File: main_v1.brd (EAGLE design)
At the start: 79.4 x 80.6 mm, 44 parts, among them IC1 MEGA8-P, IC2 7805TV, IC4 MC33063/MC34063P, IC5 MAX6921, IC6 MAX6921

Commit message: Fix some trace widths
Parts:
- R13: device resistor:0204V -> resistor:0207/10
- moved R13 23.5 mm to (29.5, 58.4), turned to 270 degrees
- moved R15 0.32 mm to (31.4, 70.5)
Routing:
- net ESP_RST: track 38.2 -> 33.7 mm
- net VCC: track 194.7 -> 191.3 mm
- net GND: track 312.2 -> 311.6 mm
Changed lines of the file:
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@@
 <setting verticaltext="up"/>
 </settings>
-<grid distance="0.025" unitdist="inch" unit="inch" style="dots" multiple="1" display="yes" altdistance="0.0125" altunitdist="inch" altunit="inch"/>
+<grid distance="0.025" unitdist="inch" unit="inch" style="dots" multiple="1" display="no" altdistance="0.0125" altunitdist="inch" altunit="inch"/>
 <layers>
 <layer number="1" name="Top" color="4" fill="1" visible="no" active="yes"/>
@@
 <attribute name="VALUE" x="72.6694" y="63.6524" size="0.9906" layer="27" ratio="10"/>
 </element>
-<element name="R13" library="resistor" package="0204V" value="" x="34.925" y="35.56" rot="R180"/>
+<element name="R13" library="resistor" package="0207/10" value="" x="29.5275" y="58.42" smashed="yes" rot="R270">
+<attribute name="NAME" x="29.1465" y="60.198" size="1.27" layer="25" ratio="10" rot="R270"/>
+<attribute name="VALUE" x="28.8925" y="60.6806" size="1.27" layer="27" ratio="10" rot="R270"/>
+</element>
 <element name="R14" library="resistor" package="0204/7" value="" x="29.845" y="48.26" smashed="yes">
 <attribute name="NAME" x="28.575" y="47.6504" size="0.9906" layer="25" ratio="10"/>
 <attribute name="VALUE" x="28.2194" y="47.7774" size="0.9906" layer="27" ratio="10"/>
 </element>
-<element name="R15" library="resistor" package="0204/7" value="4k7" x="31.115" y="70.485" smashed="yes" rot="R270">
-<attribute name="NAME" x="30.3784" y="71.9836" size="1.27" layer="25" ratio="10" rot="R270"/>
-<attribute name="VALUE" x="28.8036" y="72.6186" size="1.27" layer="27" ratio="10" rot="R270"/>
+<element name="R15" library="resistor" package="0204/7" value="4k7" x="31.4325" y="70.485" smashed="yes" rot="R270">
+<attribute name="NAME" x="30.6959" y="71.9836" size="1.27" layer="25" ratio="10" rot="R270"/>
+<attribute name="VALUE" x="29.1211" y="72.6186" size="1.27" layer="27" ratio="10" rot="R270"/>
 </element>
 <element name="R16" library="resistor" package="0204/7" value="4k7" x="26.3525" y="46.355" smashed="yes">
@@
 <attribute name="VALUE" x="24.7269" y="45.8724" size="0.9906" layer="27" ratio="10"/>
 </element>
-<element name="ICSP_ESP" library="con-lstb" package="MA05-1" value="" x="33.02" y="58.42" rot="R90">
+<element name="ICSP_ESP" library="con-lstb" package="MA05-1" value="" x="33.02" y="58.42" smashed="yes" rot="R90">
 <attribute name="OC_NEWARK" value="unknown" x="33.02" y="58.42" size="1.778" layer="27" rot="R90" display="off"/>
 <attribute name="MPN" value="" x="33.02" y="58.42" size="1.778" layer="27" rot="R90" display="off"/>
 <attribute name="MF" value="" x="33.02" y="58.42" size="1.778" layer="27" rot="R90" display="off"/>
 <attribute name="OC_FARNELL" value="unknown" x="33.02" y="58.42" size="1.778" layer="27" rot="R90" display="off"/>
+<attribute name="NAME" x="35.814" y="59.055" size="1.27" layer="25" ratio="10" rot="R90"/>
+<attribute name="VALUE" x="35.941" y="55.88" size="1.27" layer="27" ratio="10" rot="R90"/>
 </element>
 <element name="ESP8266" library="adafruit" package="2X04" value="" x="33.655" y="41.91" smashed="yes" rot="R270">
@@
 <via x="26.67" y="21.59" extent="1-16" drill="0.8128" diameter="1.27" shape="octagon"/>
 <wire x1="26.67" y1="33.655" x2="26.67" y2="21.59" width="0.4064" layer="1"/>
-<wire x1="29.845" y1="72.39" x2="29.845" y2="68.58" width="0.4064" layer="16"/>
+<wire x1="29.845" y1="71.755" x2="29.845" y2="68.58" width="0.4064" layer="16"/>
 <contactref element="IC3" pad="6"/>
 <via x="24.13" y="6.35" extent="1-16" drill="0.8128" diameter="1.27" shape="octagon"/>
 <wire x1="29.845" y1="68.58" x2="29.21" y2="67.945" width="0.4064" layer="16"/>
-<wire x1="29.21" y1="67.945" x2="29.21" y2="53.0225" width="0.4064" layer="16"/>
+<wire x1="29.21" y1="67.945" x2="29.21" y2="63.5" width="0.4064" layer="16"/>
+<wire x1="29.21" y1="63.5" x2="29.21" y2="54.9275" width="0.4064" layer="16"/>
+<wire x1="29.21" y1="54.9275" x2="27.94" y2="53.6575" width="0.4064" layer="16"/>
+<wire x1="27.94" y1="53.6575" x2="27.94" y2="51.7525" width="0.4064" layer="16"/>
 <wire x1="24.13" y1="6.35" x2="24.13" y2="27.94" width="0.4064" layer="1"/>
 <via x="24.13" y="27.94" extent="1-16" drill="0.8128" diameter="1.27" shape="octagon"/>
@@
 <wire x1="35.56" y1="31.75" x2="37.1475" y2="31.75" width="0.4064" layer="16"/>
 <wire x1="37.1475" y1="31.75" x2="38.4175" y2="33.02" width="0.4064" layer="16"/>
-<wire x1="35.56" y1="31.75" x2="34.6075" y2="32.7025" width="0.4064" layer="16"/>
-<wire x1="34.6075" y1="32.7025" x2="31.4325" y2="35.8775" width="0.4064" layer="16"/>
+<wire x1="35.56" y1="31.75" x2="31.4325" y2="35.8775" width="0.4064" layer="16"/>
 <wire x1="31.4325" y1="35.8775" x2="30.48" y2="36.83" width="0.4064" layer="16"/>
 <wire x1="30.48" y1="36.83" x2="25.4" y2="36.83" width="0.4064" layer="16"/>
@@
 <wire x1="38.735" y1="74.295" x2="37.465" y2="75.565" width="0.4064" layer="16"/>
 <wire x1="37.465" y1="75.565" x2="34.29" y2="75.565" width="0.4064" layer="16"/>
-<wire x1="34.29" y1="75.565" x2="31.75" y2="75.565" width="0.4064" layer="16"/>
+<wire x1="34.29" y1="75.565" x2="32.0675" y2="75.565" width="0.4064" layer="16"/>
 <wire x1="22.5425" y1="46.355" x2="25.24125" y2="49.05375" width="0.4064" layer="16"/>
-<wire x1="25.24125" y1="49.05375" x2="29.21" y2="53.0225" width="0.4064" layer="16"/>
-<wire x1="36.195" y1="35.56" x2="36.195" y2="34.29" width="0.4064" layer="16"/>
-<wire x1="36.195" y1="34.29" x2="34.6075" y2="32.7025" width="0.4064" layer="16"/>
+<wire x1="25.24125" y1="49.05375" x2="27.94" y2="51.7525" width="0.4064" layer="16"/>
 <wire x1="22.5425" y1="46.355" x2="22.5425" y2="45.72" width="0.4064" layer="16"/>
 <wire x1="26.035" y1="48.26" x2="25.24125" y2="49.05375" width="0.4064" layer="16"/>
@@
 <wire x1="32.385" y1="38.1" x2="32.385" y2="36.83" width="0.4064" layer="16"/>
 <wire x1="32.385" y1="36.83" x2="31.4325" y2="35.8775" width="0.4064" layer="16"/>
-<wire x1="29.845" y1="72.39" x2="31.115" y2="73.66" width="0.4064" layer="16"/>
-<wire x1="31.115" y1="73.66" x2="31.115" y2="74.295" width="0.4064" layer="16"/>
-<wire x1="31.115" y1="74.93" x2="31.75" y2="75.565" width="0.4064" layer="16"/>
-<wire x1="31.115" y1="74.93" x2="31.115" y2="74.295" width="0.4064" layer="16"/>
+<wire x1="29.845" y1="71.755" x2="31.4325" y2="73.3425" width="0.4064" layer="16"/>
+<wire x1="31.4325" y1="73.3425" x2="31.4325" y2="74.295" width="0.4064" layer="16"/>
+<wire x1="31.4325" y1="74.93" x2="32.0675" y2="75.565" width="0.4064" layer="16"/>
+<wire x1="31.4325" y1="74.93" x2="31.4325" y2="74.295" width="0.4064" layer="16"/>
+<wire x1="29.5275" y1="63.5" x2="29.21" y2="63.5" width="0.4064" layer="16"/>
 </signal>
 <signal name="GND">
@@
 <wire x1="34.29" y1="73.025" x2="36.83" y2="73.025" width="0.4064" layer="16"/>
 <wire x1="34.29" y1="64.77" x2="33.655" y2="65.405" width="0.4064" layer="16"/>
-<wire x1="33.655" y1="65.405" x2="30.48" y2="65.405" width="0.4064" layer="16"/>
-<wire x1="30.48" y1="65.405" x2="29.845" y2="66.04" width="0.4064" layer="16"/>
-<wire x1="29.845" y1="66.04" x2="29.845" y2="67.31" width="0.4064" layer="16"/>
-<wire x1="29.845" y1="67.31" x2="30.48" y2="67.945" width="0.4064" layer="16"/>
-<wire x1="30.48" y1="67.945" x2="33.02" y2="67.945" width="0.4064" layer="16"/>
+<wire x1="33.655" y1="65.405" x2="30.7975" y2="65.405" width="0.4064" layer="16"/>
+<wire x1="30.7975" y1="65.405" x2="30.1625" y2="66.04" width="0.4064" layer="16"/>
+<wire x1="30.1625" y1="66.04" x2="30.1625" y2="67.31" width="0.4064" layer="16"/>
+<wire x1="30.1625" y1="67.31" x2="30.7975" y2="67.945" width="0.4064" layer="16"/>
+<wire x1="30.7975" y1="67.945" x2="33.02" y2="67.945" width="0.4064" layer="16"/>
 <wire x1="33.02" y1="67.945" x2="34.29" y2="69.215" width="0.4064" layer="16"/>
 <wire x1="34.29" y1="69.215" x2="34.29" y2="73.025" width="0.4064" layer="16"/>
@@
 <wire x1="36.83" y1="44.1325" x2="36.83" y2="41.275" width="0.4064" layer="16"/>
 <wire x1="36.83" y1="41.275" x2="36.195" y2="40.64" width="0.4064" layer="16"/>
-<wire x1="31.115" y1="66.675" x2="33.655" y2="66.675" width="0.4064" layer="16"/>
+<wire x1="31.4325" y1="66.675" x2="33.655" y2="66.675" width="0.4064" layer="16"/>
 </signal>
 <signal name="ESP_RST">
 <contactref element="ICSP_ESP" pad="5"/>
-<wire x1="33.02" y1="39.37" x2="32.385" y2="39.37" width="0.4064" layer="16"/>
-<wire x1="32.385" y1="39.37" x2="27.94" y2="39.37" width="0.4064" layer="16"/>
+<wire x1="31.115" y1="39.37" x2="27.94" y2="39.37" width="0.4064" layer="16"/>
 <wire x1="27.94" y1="39.37" x2="26.9875" y2="40.3225" width="0.4064" layer="16"/>
 <wire x1="26.9875" y1="40.3225" x2="26.9875" y2="46.0375" width="0.4064" layer="16"/>
@@
 <contactref element="R13" pad="2"/>
 <contactref element="ESP8266" pad="5"/>
-<wire x1="33.655" y1="35.56" x2="33.655" y2="38.735" width="0.4064" layer="16"/>
-<wire x1="33.02" y1="39.37" x2="33.655" y2="38.735" width="0.4064" layer="16"/>
-<wire x1="32.385" y1="40.64" x2="32.385" y2="39.37" width="0.4064" layer="16"/>
+<wire x1="32.385" y1="40.64" x2="31.115" y2="39.37" width="0.4064" layer="16"/>
 <wire x1="33.02" y1="63.5" x2="31.75" y2="63.5" width="0.4064" layer="16"/>
 <wire x1="31.75" y1="63.5" x2="30.48" y2="62.23" width="0.4064" layer="16"/>
-<wire x1="30.48" y1="62.23" x2="30.48" y2="49.53" width="0.4064" layer="16"/>
+<wire x1="30.48" y1="62.23" x2="30.48" y2="53.34" width="0.4064" layer="16"/>
+<wire x1="30.48" y1="53.34" x2="30.48" y2="49.53" width="0.4064" layer="16"/>
+<wire x1="29.5275" y1="53.34" x2="30.48" y2="53.34" width="0.4064" layer="16"/>
 </signal>
 </signals>

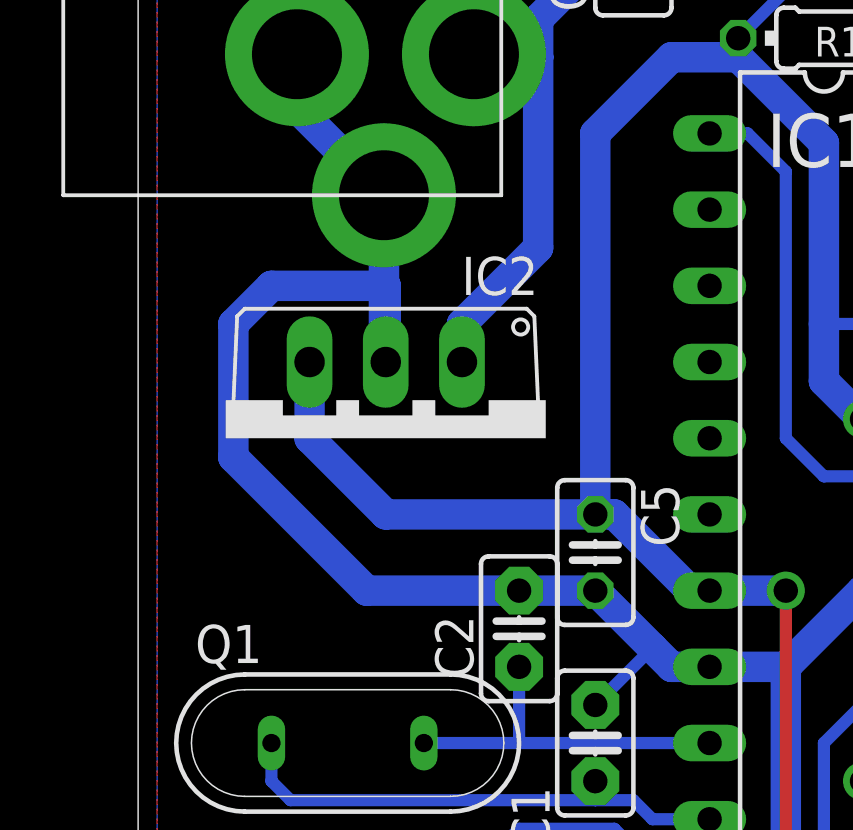
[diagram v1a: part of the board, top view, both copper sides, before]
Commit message: Replace LM7805 with LD33v
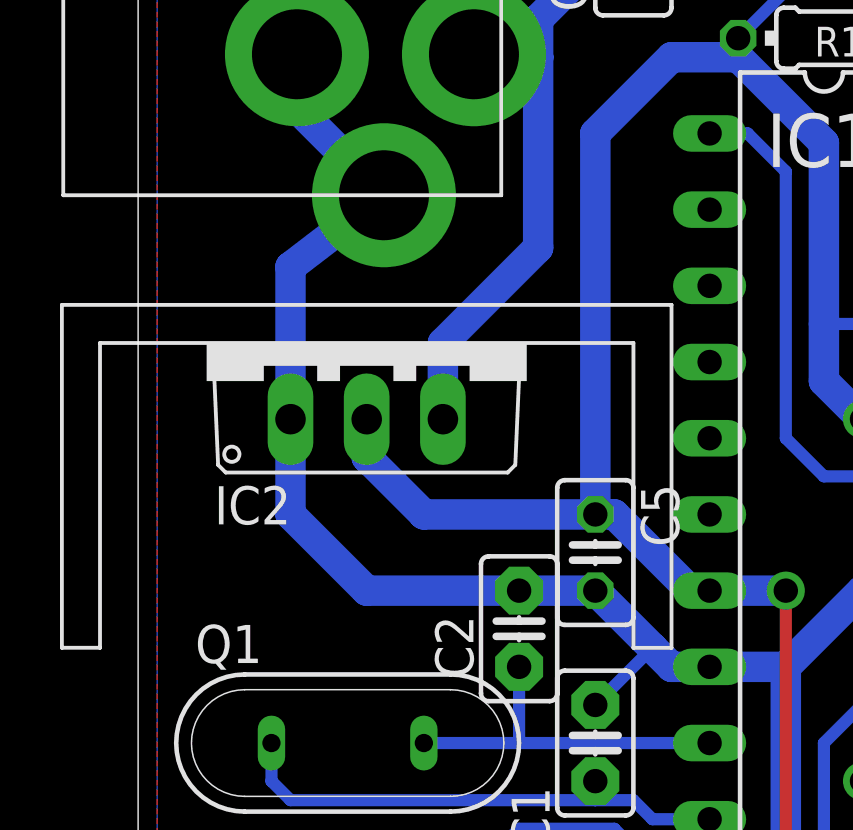
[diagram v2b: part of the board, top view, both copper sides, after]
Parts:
- IC2: value 7805TV -> LD33V05TV; device linear:TO220V -> ld33v:TO220V
- moved IC2 3.24 mm to (10.2, 36.2), turned to 0 degrees
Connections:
- net +5V: now also IC2.3; no longer IC2.1
- net GND: now also IC2.1; no longer IC2.2
- net VCC: now also IC2.2; no longer IC2.3
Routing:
- net GND: track 311.6 -> 302.9 mm
- net VCC: track 191.3 -> 187.9 mm
- net +5V: track 53.3 -> 55.4 mm
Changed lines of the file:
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@@
 <grid distance="0.025" unitdist="inch" unit="inch" style="dots" multiple="1" display="no" altdistance="0.0125" altunitdist="inch" altunit="inch"/>
 <layers>
-<layer number="1" name="Top" color="4" fill="1" visible="no" active="yes"/>
+<layer number="1" name="Top" color="4" fill="1" visible="yes" active="yes"/>
 <layer number="2" name="Route2" color="1" fill="3" visible="no" active="no"/>
 <layer number="3" name="Route3" color="4" fill="3" visible="no" active="no"/>
@@
 <attribute name="VALUE" x="22.987" y="57.023" size="1.27" layer="27" ratio="10" rot="R180"/>
 </element>
-<element name="IC2" library="linear" package="TO220V" value="7805TV" x="10.795" y="33.02" rot="R180"/>
 <element name="DCIN" library="adafruit" package="PJ-102A" value="2.1MMJACKTHM" x="4.445" y="45.72" rot="R90"/>
 <element name="C15" library="resistor" package="C025-025X050" value="" x="19.05" y="49.53" rot="R90"/>
@@
 <attribute name="VALUE" x="29.21" y="46.99" size="1.27" layer="27" rot="R270"/>
 </element>
+<element name="IC2" library="ld33v" package="TO220V" value="LD33V05TV" x="10.16" y="36.195"/>
 </elements>
 <signals>
@@
 <contactref element="C4" pad="1"/>
 <contactref element="C3" pad="1"/>
-<contactref element="IC2" pad="3"/>
-<wire x1="8.255" y1="35.56" x2="8.255" y2="33.02" width="1.016" layer="16"/>
-<wire x1="8.255" y1="33.02" x2="10.795" y2="30.48" width="1.016" layer="16"/>
-<wire x1="10.795" y1="30.48" x2="17.78" y2="30.48" width="1.016" layer="16"/>
+<wire x1="12.065" y1="30.48" x2="17.78" y2="30.48" width="1.016" layer="16"/>
 <wire x1="33.02" y1="22.86" x2="29.21" y2="22.86" width="1.016" layer="16"/>
 <wire x1="36.83" y1="17.78" x2="33.02" y2="21.59" width="1.016" layer="16"/>
@@
 <wire x1="31.4325" y1="74.93" x2="31.4325" y2="74.295" width="0.4064" layer="16"/>
 <wire x1="29.5275" y1="63.5" x2="29.21" y2="63.5" width="0.4064" layer="16"/>
+<wire x1="12.065" y1="30.48" x2="10.16" y2="32.385" width="1.016" layer="16"/>
+<contactref element="IC2" pad="2"/>
+<wire x1="10.16" y1="32.385" x2="10.16" y2="33.655" width="1.016" layer="16"/>
 </signal>
 <signal name="GND">
@@
 <contactref element="IC4" pad="2"/>
 <contactref element="IC4" pad="4"/>
-<contactref element="IC2" pad="2"/>
 <contactref element="DCIN" pad="RING_SW"/>
 <contactref element="DCIN" pad="RING"/>
@@
 <wire x1="21.2725" y1="50.8" x2="21.59" y2="50.8" width="1.016" layer="16"/>
 <wire x1="9.525" y1="50.8" x2="19.05" y2="50.8" width="1.016" layer="16"/>
-<wire x1="10.735" y1="41.12" x2="10.735" y2="35.62" width="1.016" layer="16"/>
-<wire x1="10.735" y1="35.62" x2="10.795" y2="35.56" width="1.016" layer="16"/>
-<wire x1="10.795" y1="35.56" x2="10.795" y2="38.1" width="1.016" layer="16"/>
-<wire x1="10.795" y1="38.1" x2="6.985" y2="38.1" width="1.016" layer="16"/>
-<wire x1="6.985" y1="38.1" x2="5.715" y2="36.83" width="1.016" layer="16"/>
 <wire x1="15.24" y1="27.94" x2="17.78" y2="27.94" width="1.016" layer="16"/>
 <wire x1="17.78" y1="27.94" x2="19.685" y2="26.035" width="1.016" layer="16"/>
@@
 <contactref element="IC3" pad="8"/>
 <wire x1="15.24" y1="27.94" x2="10.16" y2="27.94" width="1.016" layer="16"/>
-<wire x1="10.16" y1="27.94" x2="5.715" y2="32.385" width="1.016" layer="16"/>
-<wire x1="5.715" y1="32.385" x2="5.715" y2="36.83" width="1.016" layer="16"/>
+<wire x1="10.16" y1="27.94" x2="7.62" y2="30.48" width="1.016" layer="16"/>
 <wire x1="17.78" y1="24.13" x2="19.685" y2="26.035" width="0.4064" layer="16"/>
 <wire x1="24.13" y1="8.255" x2="19.685" y2="8.255" width="1.016" layer="16"/>
@@
 <wire x1="33.02" y1="67.945" x2="34.29" y2="69.215" width="0.4064" layer="16"/>
 <wire x1="34.29" y1="69.215" x2="34.29" y2="73.025" width="0.4064" layer="16"/>
+<contactref element="IC2" pad="1"/>
+<wire x1="7.62" y1="30.48" x2="7.62" y2="33.655" width="1.016" layer="16"/>
+<wire x1="7.62" y1="33.655" x2="7.62" y2="38.735" width="1.016" layer="16"/>
+<wire x1="7.62" y1="38.735" x2="10.735" y2="41.12" width="1.016" layer="16"/>
 </signal>
 <signal name="MOSI">
@@
 </signal>
 <signal name="+5V">
-<contactref element="IC2" pad="1"/>
 <contactref element="IC4" pad="6"/>
 <contactref element="R6" pad="2"/>
@@
 <wire x1="15.875" y1="46.99" x2="15.875" y2="45.72" width="1.016" layer="16"/>
 <wire x1="15.875" y1="45.72" x2="15.875" y2="39.37" width="1.016" layer="16"/>
-<wire x1="15.875" y1="39.37" x2="13.335" y2="36.83" width="1.016" layer="16"/>
-<wire x1="13.335" y1="36.83" x2="13.335" y2="35.56" width="1.016" layer="16"/>
+<wire x1="15.875" y1="39.37" x2="12.7" y2="36.195" width="1.016" layer="16"/>
 <wire x1="13.735" y1="45.82" x2="15.775" y2="45.82" width="1.016" layer="16"/>
 <wire x1="15.775" y1="45.82" x2="15.875" y2="45.72" width="1.016" layer="16"/>
+<contactref element="IC2" pad="3"/>
+<wire x1="12.7" y1="36.195" x2="12.7" y2="33.655" width="1.016" layer="16"/>
 </signal>
 <signal name="SPARE1">

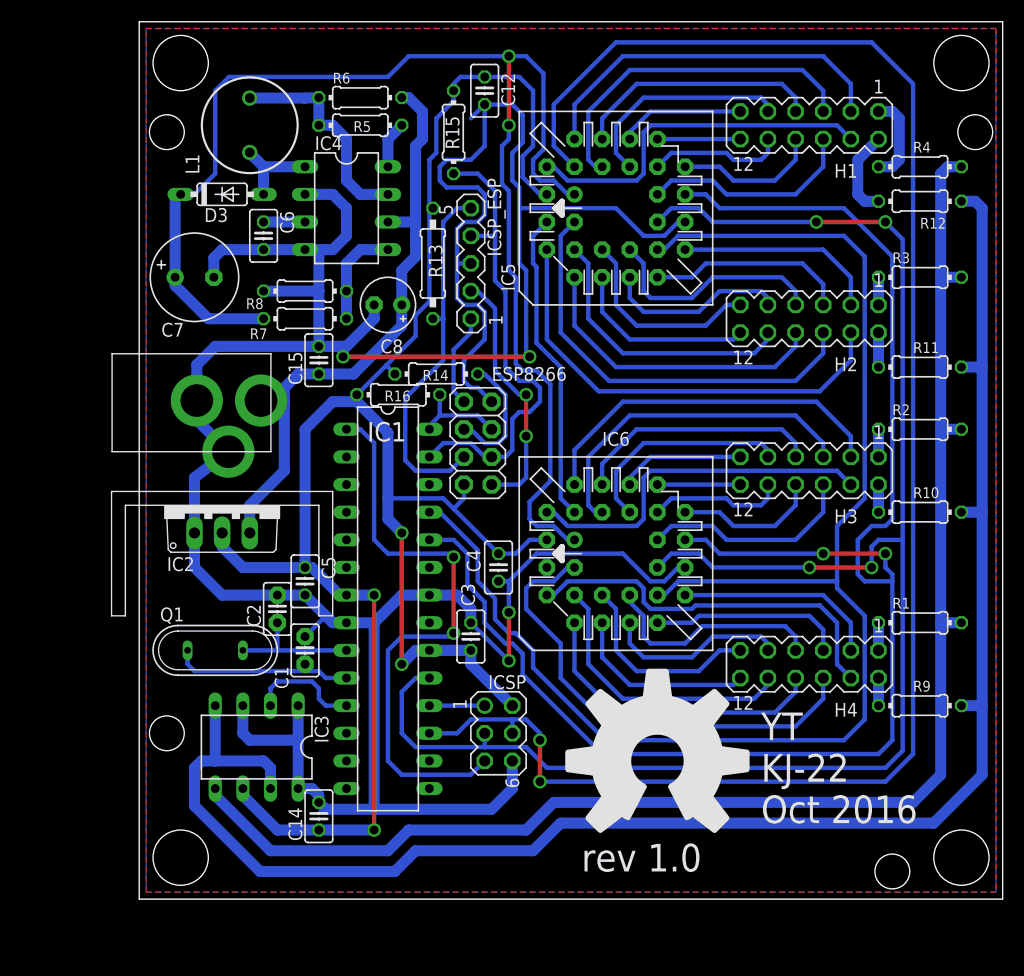
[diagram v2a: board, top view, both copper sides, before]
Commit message: swapped a few ground traces around
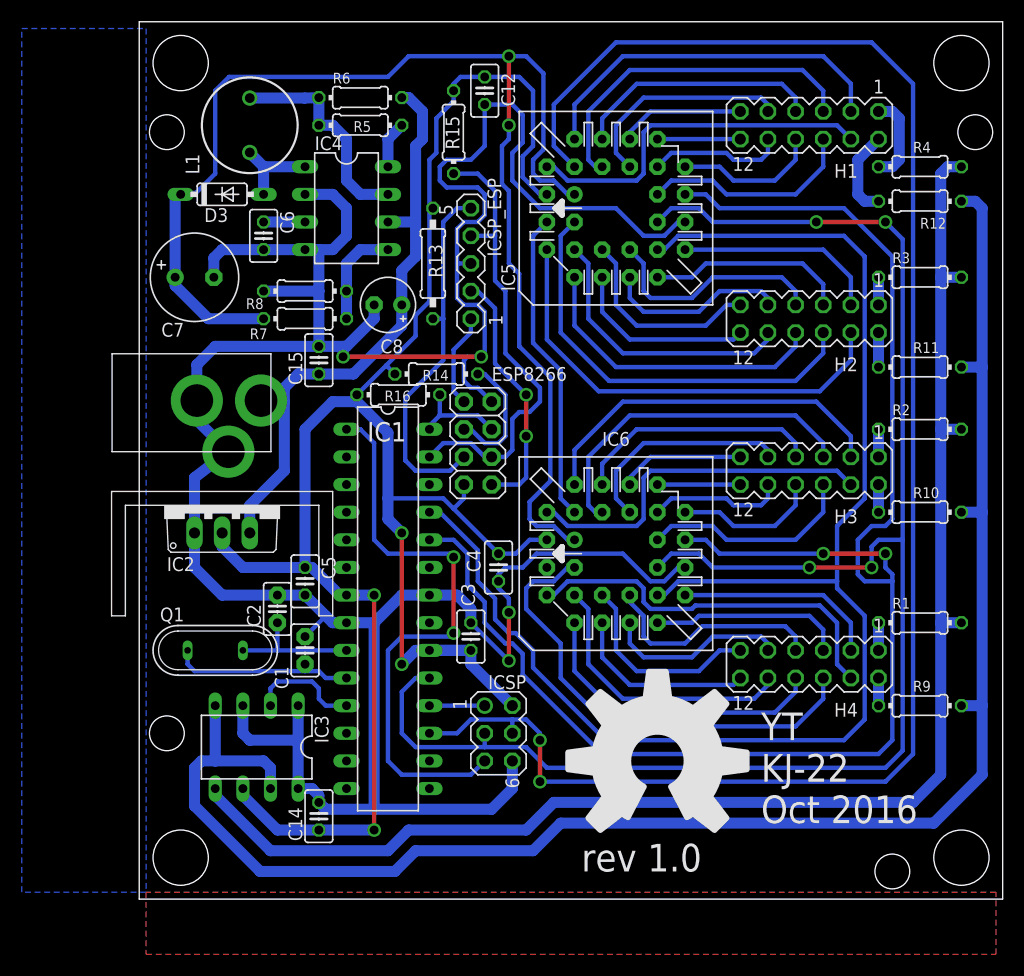
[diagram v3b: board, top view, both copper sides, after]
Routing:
- net GND: track 302.9 -> 283.0 mm
- net SDA: track 43.5 -> 42.8 mm
- net VBB: track 128.1 -> 127.3 mm
